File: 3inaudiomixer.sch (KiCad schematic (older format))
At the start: 41 parts, among them J1 AudioJack3, J2 AudioJack3, J3 AudioJack3, J4 AudioJack3, J5 Conn_01x03_Female, U1 LF353D, U2 LF353D, U3 L78L05_SOT89, U4 L79L05_SOT89

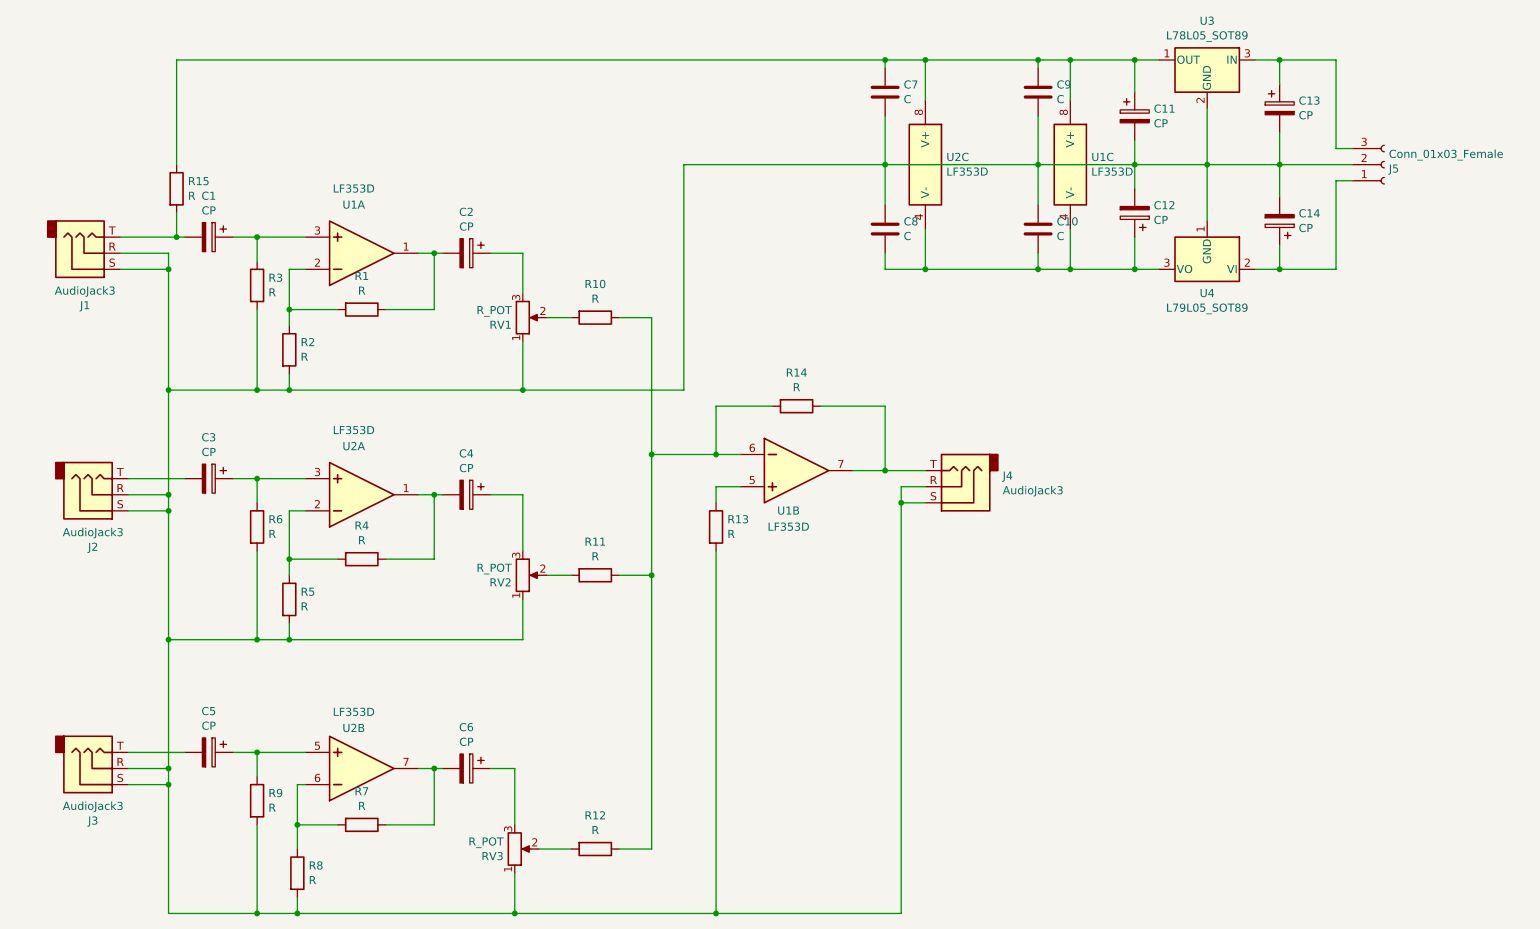
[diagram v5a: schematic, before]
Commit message: sch components value added
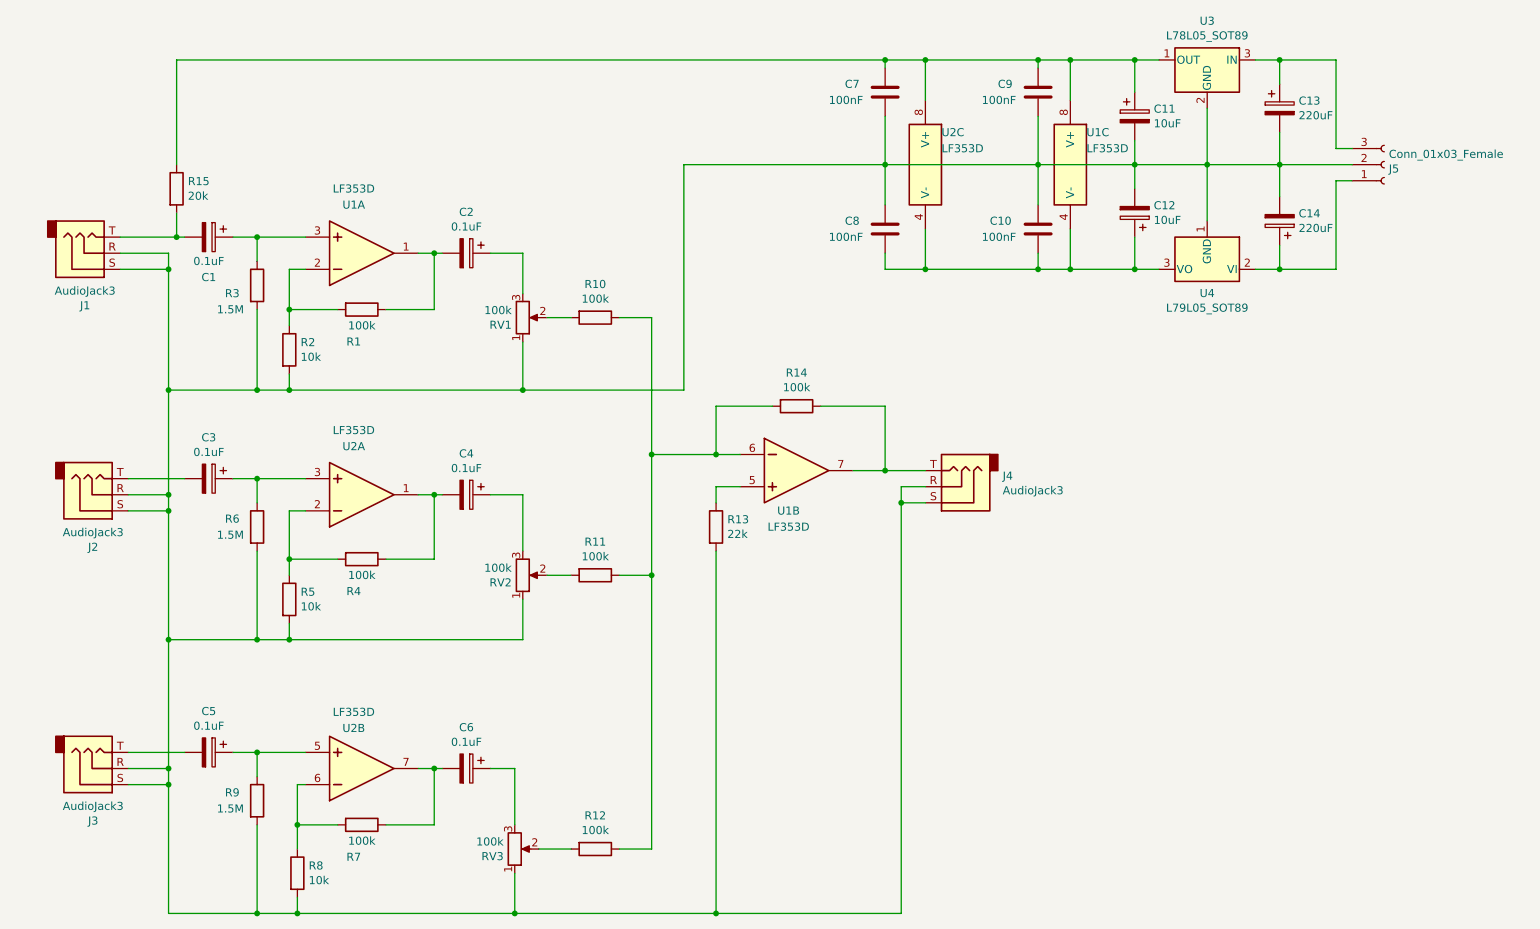
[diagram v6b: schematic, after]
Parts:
- C1, C2, C3, C4, C5, C6: value CP -> 0.1uF
- C10, C7, C8, C9: value C -> 100nF
- C11, C12: value CP -> 10uF
- C13, C14: value CP -> 220uF
- R1, R10, R11, R12, R14, R4, R7: value R -> 100k
- R13: value R -> 22k
- R15: value R -> 20k
- R2, R5, R8: value R -> 10k
- R3, R6, R9: value R -> 1.5M
- RV1, RV2, RV3: value R_POT -> 100k
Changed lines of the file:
@@
 P 4950 2400
 F 0 "RV1" H 4881 2446 50  0000 R CNN
-F 1 "R_POT" H 4881 2355 50  0000 R CNN
+F 1 "100k" H 4881 2355 50  0000 R CNN
 F 2 "Potentiometer_THT:Potentiometer_Omeg_PC16BU_Horizontal" H 4950 2400 50  0001 C CNN
 F 3 "~" H 4950 2400 50  0001 C CNN
@@
 P 4950 4000
 F 0 "RV2" H 4881 4046 50  0000 R CNN
-F 1 "R_POT" H 4881 3955 50  0000 R CNN
+F 1 "100k" H 4881 3955 50  0000 R CNN
 F 2 "Potentiometer_THT:Potentiometer_Omeg_PC16BU_Horizontal" H 4950 4000 50  0001 C CNN
 F 3 "~" H 4950 4000 50  0001 C CNN
@@
 P 4900 5700
 F 0 "RV3" H 4831 5746 50  0000 R CNN
-F 1 "R_POT" H 4831 5655 50  0000 R CNN
+F 1 "100k" H 4831 5655 50  0000 R CNN
 F 2 "Potentiometer_THT:Potentiometer_Omeg_PC16BU_Horizontal" H 4900 5700 50  0001 C CNN
 F 3 "~" H 4900 5700 50  0001 C CNN
@@
 U 3 1 60AACA7F
 P 8350 1450
-F 0 "U1" H 8480 1496 50  0000 L CNN
-F 1 "LF353D" H 8480 1405 50  0000 L CNN
+F 0 "U1" H 8450 1650 50  0000 L CNN
+F 1 "LF353D" H 8450 1550 50  0000 L CNN
 F 2 "Package_SO:SOIC-8_3.9x4.9mm_P1.27mm" H 8350 1150 50  0001 C CNN
 F 3 "http://www.ti.com/lit/ds/symlink/lf353.pdf" H 8350 1050 50  0001 C CNN
@@
 U 3 1 60AAFDA3
 P 7450 1450
-F 0 "U2" H 7580 1496 50  0000 L CNN
-F 1 "LF353D" H 7580 1405 50  0000 L CNN
+F 0 "U2" H 7550 1650 50  0000 L CNN
+F 1 "LF353D" H 7550 1550 50  0000 L CNN
 F 2 "Package_SO:SOIC-8_3.9x4.9mm_P1.27mm" H 7450 1150 50  0001 C CNN
 F 3 "http://www.ti.com/lit/ds/symlink/lf353.pdf" H 7450 1050 50  0001 C CNN
@@
 U 1 1 60B01F57
 P 3300 2200
-F 0 "R3" H 3370 2246 50  0000 L CNN
-F 1 "R" H 3370 2155 50  0000 L CNN
+F 0 "R3" H 3100 2150 50  0000 L CNN
+F 1 "1.5M" H 3050 2050 50  0000 L CNN
 F 2 "Resistor_SMD:R_0805_2012Metric_Pad1.15x1.40mm_HandSolder" V 3230 2200 50  0001 C CNN
 F 3 "~" H 3300 2200 50  0001 C CNN
@@
 P 3500 2600
 F 0 "R2" H 3570 2646 50  0000 L CNN
-F 1 "R" H 3570 2555 50  0000 L CNN
+F 1 "10k" H 3570 2555 50  0000 L CNN
 F 2 "Resistor_SMD:R_0805_2012Metric_Pad1.15x1.40mm_HandSolder" V 3430 2600 50  0001 C CNN
 F 3 "~" H 3500 2600 50  0001 C CNN
@@
 U 1 1 60B05409
 P 3950 2350
-F 0 "R1" V 3743 2350 50  0000 C CNN
-F 1 "R" V 3834 2350 50  0000 C CNN
+F 0 "R1" V 4150 2300 50  0000 C CNN
+F 1 "100k" V 4050 2350 50  0000 C CNN
 F 2 "Resistor_SMD:R_0805_2012Metric_Pad1.15x1.40mm_HandSolder" V 3880 2350 50  0001 C CNN
 F 3 "~" H 3950 2350 50  0001 C CNN
@@
 P 4600 2000
 F 0 "C2" V 4345 2000 50  0000 C CNN
-F 1 "CP" V 4436 2000 50  0000 C CNN
+F 1 "0.1uF" V 4436 2000 50  0000 C CNN
 F 2 "Capacitor_SMD:C_0805_2012Metric_Pad1.15x1.40mm_HandSolder" H 4638 1850 50  0001 C CNN
 F 3 "~" H 4600 2000 50  0001 C CNN
@@
 U 1 1 60B299D3
 P 3000 1900
-F 0 "C1" V 2745 1900 50  0000 C CNN
-F 1 "CP" V 2836 1900 50  0000 C CNN
+F 0 "C1" V 3250 1900 50  0000 C CNN
+F 1 "0.1uF" V 3150 1900 50  0000 C CNN
 F 2 "Capacitor_SMD:C_0805_2012Metric_Pad1.15x1.40mm_HandSolder" H 3038 1750 50  0001 C CNN
 F 3 "~" H 3000 1900 50  0001 C CNN
@@
 U 1 1 60B455E7
 P 3300 3700
-F 0 "R6" H 3370 3746 50  0000 L CNN
-F 1 "R" H 3370 3655 50  0000 L CNN
+F 0 "R6" H 3100 3750 50  0000 L CNN
+F 1 "1.5M" H 3050 3650 50  0000 L CNN
 F 2 "Resistor_SMD:R_0805_2012Metric_Pad1.15x1.40mm_HandSolder" V 3230 3700 50  0001 C CNN
 F 3 "~" H 3300 3700 50  0001 C CNN
@@
 P 3500 4150
 F 0 "R5" H 3570 4196 50  0000 L CNN
-F 1 "R" H 3570 4105 50  0000 L CNN
+F 1 "10k" H 3570 4105 50  0000 L CNN
 F 2 "Resistor_SMD:R_0805_2012Metric_Pad1.15x1.40mm_HandSolder" V 3430 4150 50  0001 C CNN
 F 3 "~" H 3500 4150 50  0001 C CNN
@@
 U 1 1 60B47C4E
 P 3950 3900
-F 0 "R4" V 3743 3900 50  0000 C CNN
-F 1 "R" V 3834 3900 50  0000 C CNN
+F 0 "R4" V 4150 3850 50  0000 C CNN
+F 1 "100k" V 4050 3900 50  0000 C CNN
 F 2 "Resistor_SMD:R_0805_2012Metric_Pad1.15x1.40mm_HandSolder" V 3880 3900 50  0001 C CNN
 F 3 "~" H 3950 3900 50  0001 C CNN
@@
 P 4600 3500
 F 0 "C4" V 4345 3500 50  0000 C CNN
-F 1 "CP" V 4436 3500 50  0000 C CNN
+F 1 "0.1uF" V 4436 3500 50  0000 C CNN
 F 2 "Capacitor_SMD:C_0805_2012Metric_Pad1.15x1.40mm_HandSolder" H 4638 3350 50  0001 C CNN
 F 3 "~" H 4600 3500 50  0001 C CNN
@@
 P 3000 3400
 F 0 "C3" V 2745 3400 50  0000 C CNN
-F 1 "CP" V 2836 3400 50  0000 C CNN
+F 1 "0.1uF" V 2836 3400 50  0000 C CNN
 F 2 "Capacitor_SMD:C_0805_2012Metric_Pad1.15x1.40mm_HandSolder" H 3038 3250 50  0001 C CNN
 F 3 "~" H 3000 3400 50  0001 C CNN
@@
 U 1 1 60BE429C
 P 3300 5400
-F 0 "R9" H 3370 5446 50  0000 L CNN
-F 1 "R" H 3370 5355 50  0000 L CNN
+F 0 "R9" H 3100 5450 50  0000 L CNN
+F 1 "1.5M" H 3050 5350 50  0000 L CNN
 F 2 "Resistor_SMD:R_0805_2012Metric_Pad1.15x1.40mm_HandSolder" V 3230 5400 50  0001 C CNN
 F 3 "~" H 3300 5400 50  0001 C CNN
@@
 P 3550 5850
 F 0 "R8" H 3620 5896 50  0000 L CNN
-F 1 "R" H 3620 5805 50  0000 L CNN
+F 1 "10k" H 3620 5805 50  0000 L CNN
 F 2 "Resistor_SMD:R_0805_2012Metric_Pad1.15x1.40mm_HandSolder" V 3480 5850 50  0001 C CNN
 F 3 "~" H 3550 5850 50  0001 C CNN
@@
 U 1 1 60BE6705
 P 3950 5550
-F 0 "R7" V 3743 5550 50  0000 C CNN
-F 1 "R" V 3834 5550 50  0000 C CNN
+F 0 "R7" V 4150 5500 50  0000 C CNN
+F 1 "100k" V 4050 5550 50  0000 C CNN
 F 2 "Resistor_SMD:R_0805_2012Metric_Pad1.15x1.40mm_HandSolder" V 3880 5550 50  0001 C CNN
 F 3 "~" H 3950 5550 50  0001 C CNN
@@
 P 3000 5100
 F 0 "C5" V 2745 5100 50  0000 C CNN
-F 1 "CP" V 2836 5100 50  0000 C CNN
+F 1 "0.1uF" V 2836 5100 50  0000 C CNN
 F 2 "Capacitor_SMD:C_0805_2012Metric_Pad1.15x1.40mm_HandSolder" H 3038 4950 50  0001 C CNN
 F 3 "~" H 3000 5100 50  0001 C CNN
@@
 P 4600 5200
 F 0 "C6" V 4345 5200 50  0000 C CNN
-F 1 "CP" V 4436 5200 50  0000 C CNN
+F 1 "0.1uF" V 4436 5200 50  0000 C CNN
 F 2 "Capacitor_SMD:C_0805_2012Metric_Pad1.15x1.40mm_HandSolder" H 4638 5050 50  0001 C CNN
 F 3 "~" H 4600 5200 50  0001 C CNN
@@
 P 5400 2400
 F 0 "R10" V 5193 2400 50  0000 C CNN
-F 1 "R" V 5284 2400 50  0000 C CNN
+F 1 "100k" V 5284 2400 50  0000 C CNN
 F 2 "Resistor_SMD:R_0805_2012Metric_Pad1.15x1.40mm_HandSolder" V 5330 2400 50  0001 C CNN
 F 3 "~" H 5400 2400 50  0001 C CNN
@@
 P 5400 5700
 F 0 "R12" V 5193 5700 50  0000 C CNN
-F 1 "R" V 5284 5700 50  0000 C CNN
+F 1 "100k" V 5284 5700 50  0000 C CNN
 F 2 "Resistor_SMD:R_0805_2012Metric_Pad1.15x1.40mm_HandSolder" V 5330 5700 50  0001 C CNN
 F 3 "~" H 5400 5700 50  0001 C CNN
@@
 P 5400 4000
 F 0 "R11" V 5193 4000 50  0000 C CNN
-F 1 "R" V 5284 4000 50  0000 C CNN
+F 1 "100k" V 5284 4000 50  0000 C CNN
 F 2 "Resistor_SMD:R_0805_2012Metric_Pad1.15x1.40mm_HandSolder" V 5330 4000 50  0001 C CNN
 F 3 "~" H 5400 4000 50  0001 C CNN
@@
 P 6650 2950
 F 0 "R14" V 6443 2950 50  0000 C CNN
-F 1 "R" V 6534 2950 50  0000 C CNN
+F 1 "100k" V 6534 2950 50  0000 C CNN
 F 2 "Resistor_SMD:R_0805_2012Metric_Pad1.15x1.40mm_HandSolder" V 6580 2950 50  0001 C CNN
 F 3 "~" H 6650 2950 50  0001 C CNN
@@
 P 6150 3700
 F 0 "R13" H 6220 3746 50  0000 L CNN
-F 1 "R" H 6220 3655 50  0000 L CNN
+F 1 "22k" H 6220 3655 50  0000 L CNN
 F 2 "Resistor_SMD:R_0805_2012Metric_Pad1.15x1.40mm_HandSolder" V 6080 3700 50  0001 C CNN
 F 3 "~" H 6150 3700 50  0001 C CNN
@@
 P 2800 1600
 F 0 "R15" H 2870 1646 50  0000 L CNN
-F 1 "R" H 2870 1555 50  0000 L CNN
+F 1 "20k" H 2870 1555 50  0000 L CNN
 F 2 "Resistor_SMD:R_0805_2012Metric_Pad1.15x1.40mm_HandSolder" V 2730 1600 50  0001 C CNN
 F 3 "~" H 2800 1600 50  0001 C CNN
@@
 U 1 1 60D8B58B
 P 8150 1000
-F 0 "C9" H 8265 1046 50  0000 L CNN
-F 1 "C" H 8265 955 50  0000 L CNN
+F 0 "C9" H 7900 1050 50  0000 L CNN
+F 1 "100nF" H 7800 950 50  0000 L CNN
 F 2 "Capacitor_SMD:C_0805_2012Metric_Pad1.15x1.40mm_HandSolder" H 8188 850 50  0001 C CNN
 F 3 "~" H 8150 1000 50  0001 C CNN
@@
 U 1 1 60D8C3B6
 P 8150 1850
-F 0 "C10" H 8265 1896 50  0000 L CNN
-F 1 "C" H 8265 1805 50  0000 L CNN
+F 0 "C10" H 7850 1900 50  0000 L CNN
+F 1 "100nF" H 7800 1800 50  0000 L CNN
 F 2 "Capacitor_SMD:C_0805_2012Metric_Pad1.15x1.40mm_HandSolder" H 8188 1700 50  0001 C CNN
 F 3 "~" H 8150 1850 50  0001 C CNN
@@
 U 1 1 60D8D463
 P 7200 1000
-F 0 "C7" H 7315 1046 50  0000 L CNN
-F 1 "C" H 7315 955 50  0000 L CNN
+F 0 "C7" H 6950 1050 50  0000 L CNN
+F 1 "100nF" H 6850 950 50  0000 L CNN
 F 2 "Capacitor_SMD:C_0805_2012Metric_Pad1.15x1.40mm_HandSolder" H 7238 850 50  0001 C CNN
 F 3 "~" H 7200 1000 50  0001 C CNN
@@
 U 1 1 60D901D0
 P 7200 1850
-F 0 "C8" H 7315 1896 50  0000 L CNN
-F 1 "C" H 7315 1805 50  0000 L CNN
+F 0 "C8" H 6950 1900 50  0000 L CNN
+F 1 "100nF" H 6850 1800 50  0000 L CNN
 F 2 "Capacitor_SMD:C_0805_2012Metric_Pad1.15x1.40mm_HandSolder" H 7238 1700 50  0001 C CNN
 F 3 "~" H 7200 1850 50  0001 C CNN
@@
 P 8750 1150
 F 0 "C11" H 8868 1196 50  0000 L CNN
-F 1 "CP" H 8868 1105 50  0000 L CNN
+F 1 "10uF" H 8868 1105 50  0000 L CNN
 F 2 "Capacitor_SMD:C_1206_3216Metric_Pad1.42x1.75mm_HandSolder" H 8788 1000 50  0001 C CNN
 F 3 "~" H 8750 1150 50  0001 C CNN
@@
 P 8750 1750
 F 0 "C12" H 8632 1704 50  0000 R CNN
-F 1 "CP" H 8632 1795 50  0000 R CNN
+F 1 "10uF" H 8632 1795 50  0000 R CNN
 F 2 "Capacitor_SMD:C_1206_3216Metric_Pad1.42x1.75mm_HandSolder" H 8788 1600 50  0001 C CNN
 F 3 "~" H 8750 1750 50  0001 C CNN
@@
 P 9650 1100
 F 0 "C13" H 9768 1146 50  0000 L CNN
-F 1 "CP" H 9768 1055 50  0000 L CNN
+F 1 "220uF" H 9768 1055 50  0000 L CNN
 F 2 "Capacitor_SMD:C_Elec_6.3x7.7" H 9688 950 50  0001 C CNN
 F 3 "~" H 9650 1100 50  0001 C CNN
@@
 P 9650 1800
 F 0 "C14" H 9532 1754 50  0000 R CNN
-F 1 "CP" H 9532 1845 50  0000 R CNN
+F 1 "220uF" H 9532 1845 50  0000 R CNN
 F 2 "Capacitor_SMD:C_Elec_6.3x7.7" H 9688 1650 50  0001 C CNN
 F 3 "~" H 9650 1800 50  0001 C CNN

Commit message: capacitor footprint fix
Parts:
- C11, C12: footprint Capacitor_SMD:C_1206_3216Metric_Pad1.42x1.75mm_HandSolder -> Capacitor_Tantalum_SMD:CP_EIA-3216-18_Kemet-A_Pad1.58x1.35mm_HandSolder
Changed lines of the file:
@@
 F 0 "C11" H 8868 1196 50  0000 L CNN
 F 1 "10uF" H 8868 1105 50  0000 L CNN
-F 2 "Capacitor_SMD:C_1206_3216Metric_Pad1.42x1.75mm_HandSolder" H 8788 1000 50  0001 C CNN
+F 2 "Capacitor_Tantalum_SMD:CP_EIA-3216-18_Kemet-A_Pad1.58x1.35mm_HandSolder" H 8788 1000 50  0001 C CNN
 F 3 "~" H 8750 1150 50  0001 C CNN
 	1    8750 1150
@@
 F 0 "C12" H 8632 1704 50  0000 R CNN
 F 1 "10uF" H 8632 1795 50  0000 R CNN
-F 2 "Capacitor_SMD:C_1206_3216Metric_Pad1.42x1.75mm_HandSolder" H 8788 1600 50  0001 C CNN
+F 2 "Capacitor_Tantalum_SMD:CP_EIA-3216-18_Kemet-A_Pad1.58x1.35mm_HandSolder" H 8788 1600 50  0001 C CNN
 F 3 "~" H 8750 1750 50  0001 C CNN
 	1    8750 1750

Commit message: removed voltage regulators
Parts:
- removed U3: L78L05_SOT89, Package_TO_SOT_SMD:SOT-89-3, symbol Regulator_Linear:L78L05_SOT89
- removed U4: L79L05_SOT89, Package_TO_SOT_SMD:SOT-89-3, symbol Regulator_Linear:L79L05_SOT89
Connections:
- net at C10.2, C12.1, C8.2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: now also C14.1, J5.1 (Pin_1)
- net at C11.1, C7.1, C9.1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: now also C13.1, J5.3 (Pin_3)
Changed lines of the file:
@@
-$EndComp
-$Comp
-L Regulator_Linear:L78L05_SOT89 U3
-U 1 1 60AFE4C9
-P 9200 800
-F 0 "U3" H 9200 1042 50  0000 C CNN
-F 1 "L78L05_SOT89" H 9200 951 50  0000 C CNN
-F 2 "Package_TO_SOT_SMD:SOT-89-3" H 9200 1000 50  0001 C CIN
-F 3 "http://www.st.com/content/ccc/resource/technical/document/datasheet/15/55/e5/aa/23/5b/43/fd/CD00000446.pdf/files/CD00000446.pdf/jcr:content/translations/en.CD00000446.pdf" H 9200 750 50  0001 C CNN
-	1    9200 800
-	-1   0    0    -1
-$EndComp
-$Comp
-L Regulator_Linear:L79L05_SOT89 U4
-U 1 1 60AFF106
-P 9200 2100
-F 0 "U4" H 9200 1951 50  0000 C CNN
-F 1 "L79L05_SOT89" H 9200 1860 50  0000 C CNN
-F 2 "Package_TO_SOT_SMD:SOT-89-3" H 9200 1900 50  0001 C CIN
-F 3 "http://www.farnell.com/datasheets/1827870.pdf" H 9200 2100 50  0001 C CNN
-	1    9200 2100
-	-1   0    0    -1
 $EndComp
 $Comp
@@
 	2800 1900 2850 1900
 Wire Wire Line
-	9200 1100 9200 1450
-Wire Wire Line
-	9200 1450 8750 1450
-Connection ~ 9200 1450
-Wire Wire Line
-	9200 1450 9200 1800
-Wire Wire Line
 	5950 1450 5950 2850
 Wire Wire Line
@@
 Connection ~ 8750 800
 Wire Wire Line
-	8750 800  8900 800
-Wire Wire Line
 	8750 1300 8750 1450
 Connection ~ 8750 1450
@@
 	8750 1900 8750 2100
 Connection ~ 8750 2100
-Wire Wire Line
-	8750 2100 8900 2100
 Wire Wire Line
 	2750 3500 2750 2850
@@
 $EndComp
 Wire Wire Line
-	9500 800  9650 800
-Wire Wire Line
 	9650 800  9650 950
 Wire Wire Line
-	9200 1450 9650 1450
-Wire Wire Line
 	9650 1450 9650 1250
-Wire Wire Line
-	9500 2100 9650 2100
 Wire Wire Line
 	9650 2100 9650 1950
@@
 Wire Wire Line
 	10100 1450 9650 1450
+Wire Wire Line
+	8750 1450 9650 1450
+Wire Wire Line
+	8750 800  9650 800
+Wire Wire Line
+	8750 2100 9650 2100
 $EndSCHEMATC
